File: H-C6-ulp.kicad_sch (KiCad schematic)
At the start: 80 parts, among them J1 USB_C_Receptacle_USB2.0, J2 AFC24-S24FIC-00, J3 SM02B-SRSS-TB(LF)(SN), J4 SM04B-SRSS-TB_LF__SN_, J5 OLED, Q1 Si1308, Q2 Si2301CDS, SW1 SW_Push_Dual, SW2 SW_Push_Dual, U1 ESP32-C6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

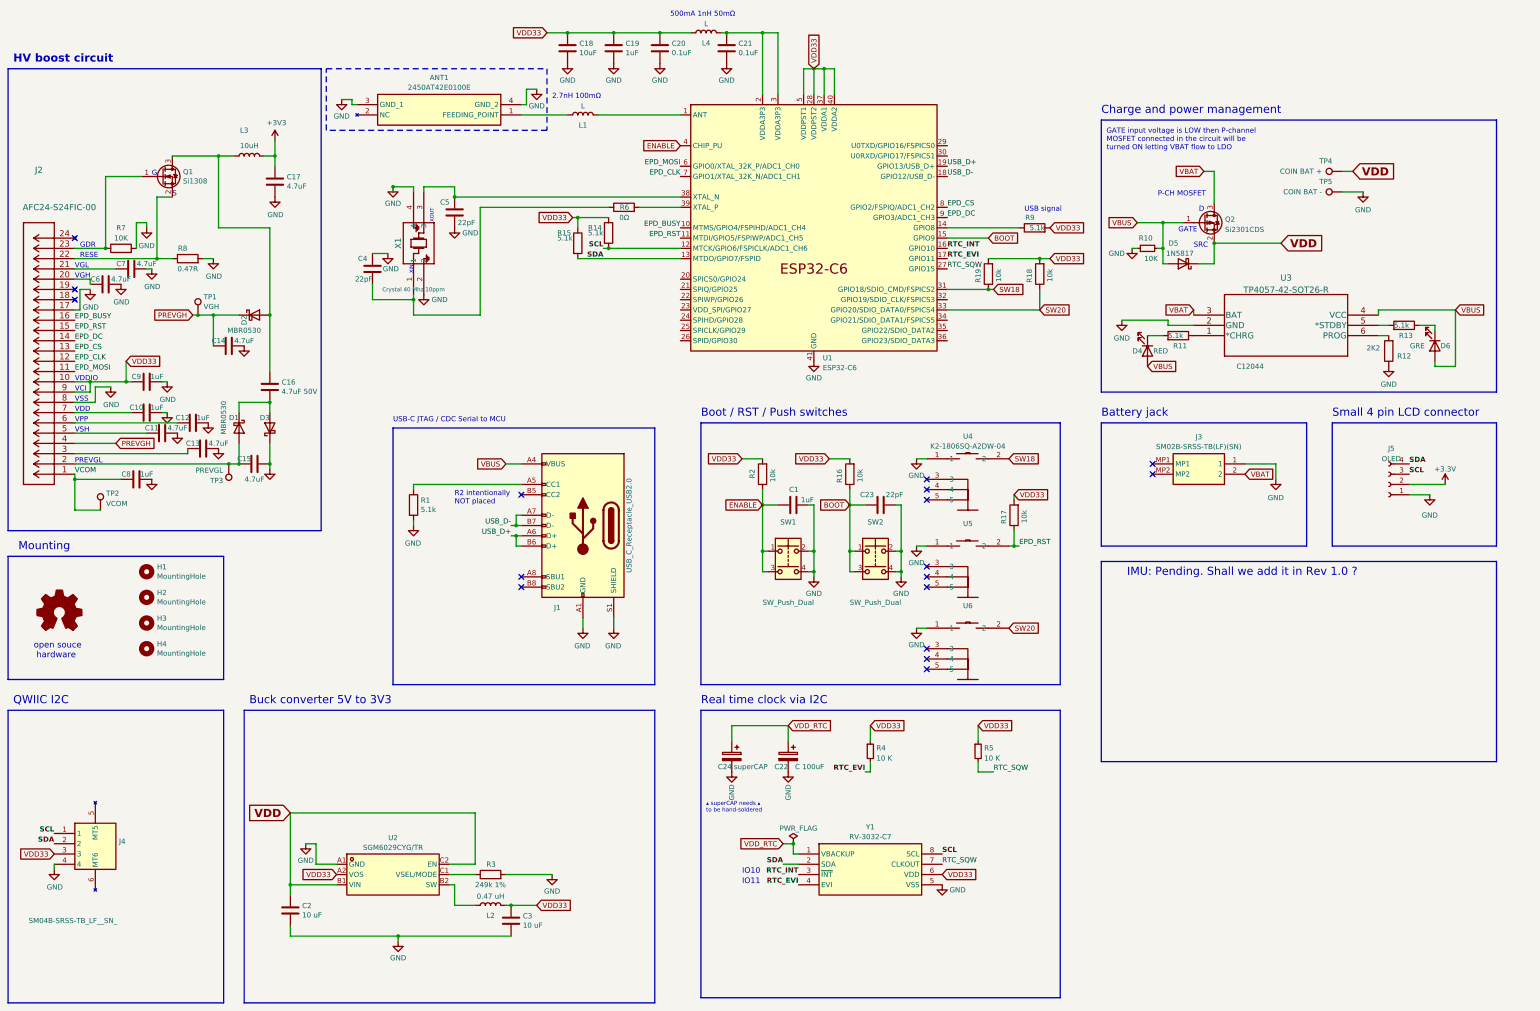
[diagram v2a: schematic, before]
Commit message: Add QSPI Flash
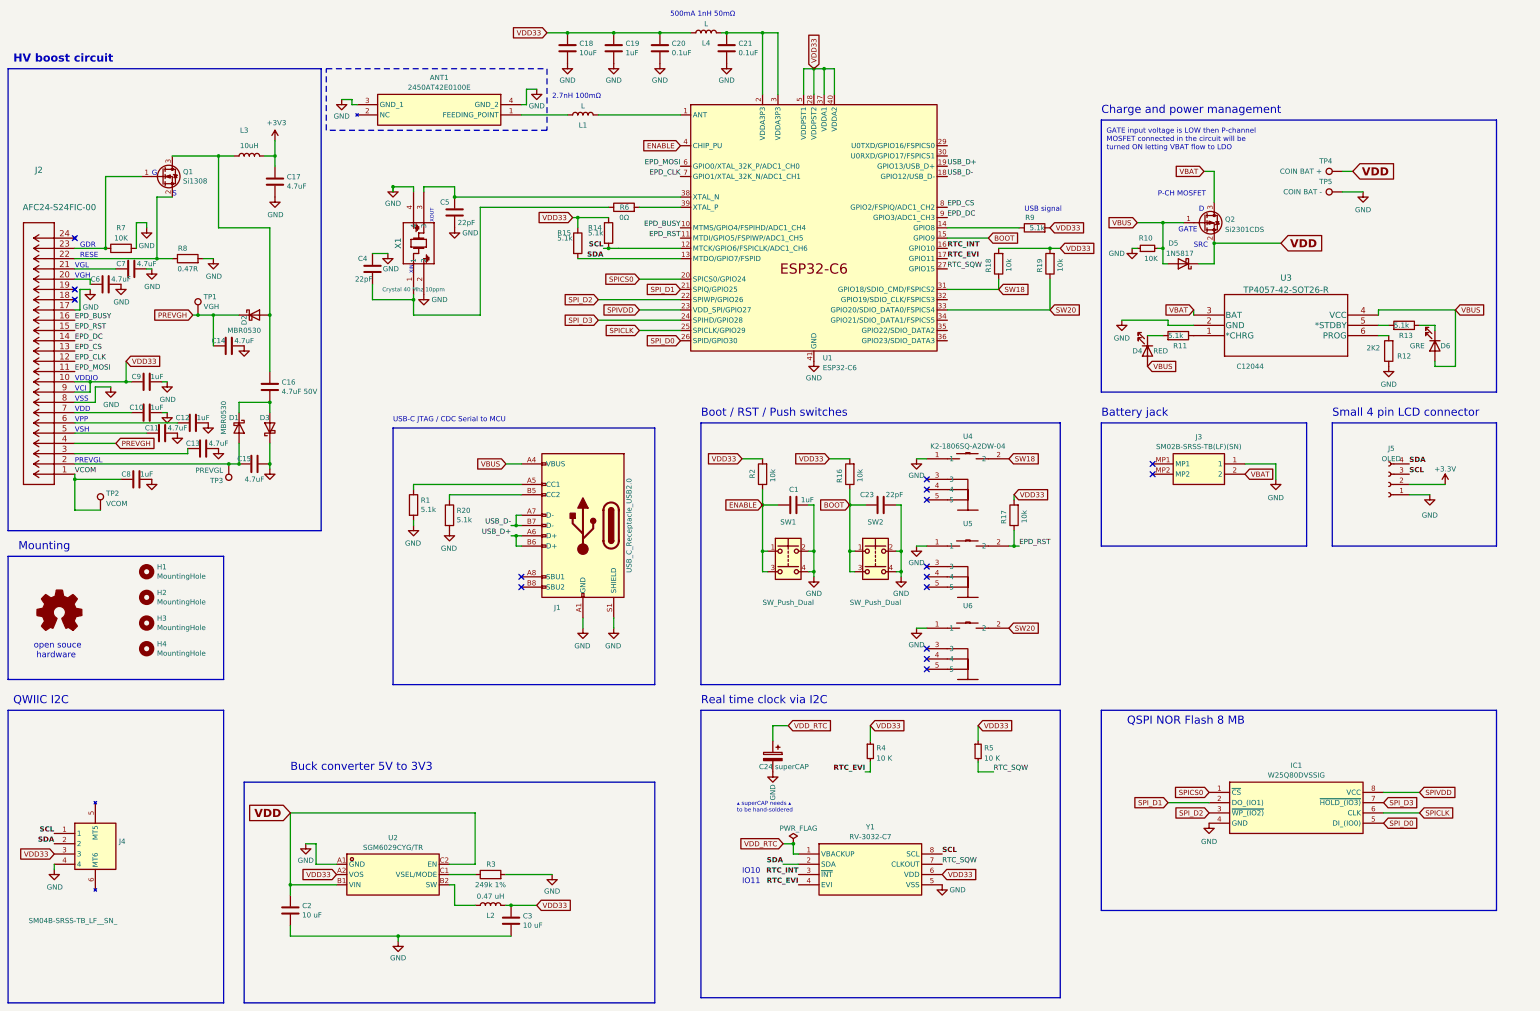
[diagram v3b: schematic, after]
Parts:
- removed C22: C 100uF, Capacitor_Tantalum_SMD:CP_EIA-3528-21_Kemet-B, symbol Device:C_Polarized
- added IC1: W25Q80DVSSIG, footprints:SOIC127P790X216-8N-FLASH, symbol FLASH:W25Q80DVSSIG
- added R20: 5.1k, Resistor_SMD:R_0603_1608Metric, symbol Device:R
- ANT1: Arrow Part Number 2450AT42E0100E -> (none); Arrow Price/Stock https://www.arrow.com/en/products/2450at42e0100e/johanson-d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 -> (none); Manufacturer_Name JOHANSON TECHNOLOGY -> (none); Manufacturer_Part_Number 2450AT42E0100E -> (none); Mouser Part Number 609-2450AT42E0100E -> (none); Mouser Price/Stock https://www.mouser.co.uk/ProductDetail/Johanson-Technology/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 -> (none)
- C1, C19: footprint Capacitor_SMD:C_0603_1608Metric -> Capacitor_SMD:C_0402_1005Metric; LCSC C5457064 -> C162161
- C2, C3: LCSC C5457064 -> C6119874
- C23, C4, C5: footprint Capacitor_SMD:C_0603_1608Metric -> Capacitor_SMD:C_0402_1005Metric; LCSC C561172 -> C5119318
- R10, R4, R5: footprint Resistor_SMD:R_0603_1608Metric -> Resistor_SMD:R_0402_1005Metric; LCSC C25804 -> C4322213
- R7: LCSC C25804 -> C4322213
- U1: LCSC C5364646 -> C5364646
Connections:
- net GND: now also IC1.4 (GND), R20.2
- net SW18: now also R18.1; no longer R19.1
- net SW20: now also R19.1; no longer R18.1
- net at J1.B5 (CC2): now also R20.1
- net SPICS0: now reaches U1.20 (SPICS0/GPIO24)
- net SPICS0: now also IC1.1 (~{CS})
- net SPI_D1: now reaches U1.21 (SPIQ/GPIO25)
- net SPI_D1: now also IC1.2 (DO_(IO1))
- net SPI_D2: now reaches U1.22 (SPIWP/GPIO26)
- net SPI_D2: now also IC1.3 (~{WP_(IO2)})
- net SPIVDD: now reaches U1.23 (VDD_SPI/GPIO27)
- net SPIVDD: now also IC1.8 (VCC)
- net SPI_D3: now reaches U1.24 (SPIHD/GPIO28)
- net SPI_D3: now also IC1.7 (~{HOLD_(IO3)})
- net SPICLK: now reaches U1.25 (SPICLK/GPIO29)
- net SPICLK: now also IC1.6 (CLK)
- net SPI_D0: now reaches U1.26 (SPID/GPIO30)
- net SPI_D0: now also IC1.5 (DI_(IO0))
- no-connect marks 17 -> 16
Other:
- note added: "QSPI NOR Flash 8 MB"
- note removed: "IMU: Pending. Shall we add it in Rev 1.0 ?"
- note removed: "R2 intentionally NOT placed"
- moved on the sheet: C24

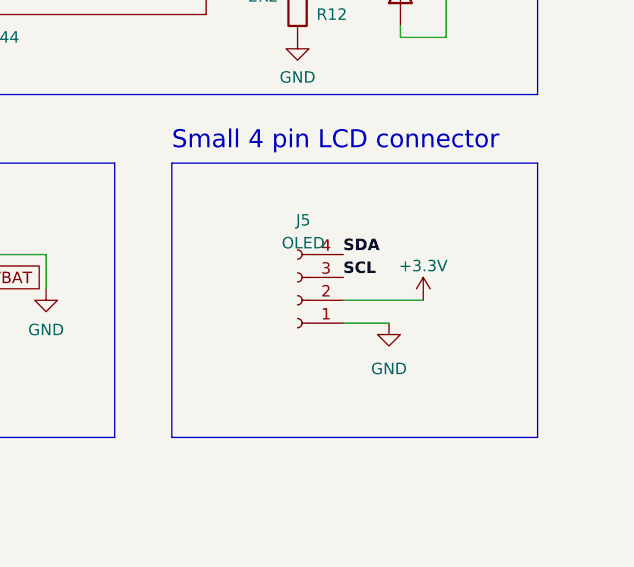
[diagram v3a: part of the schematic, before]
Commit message: Test with external flash
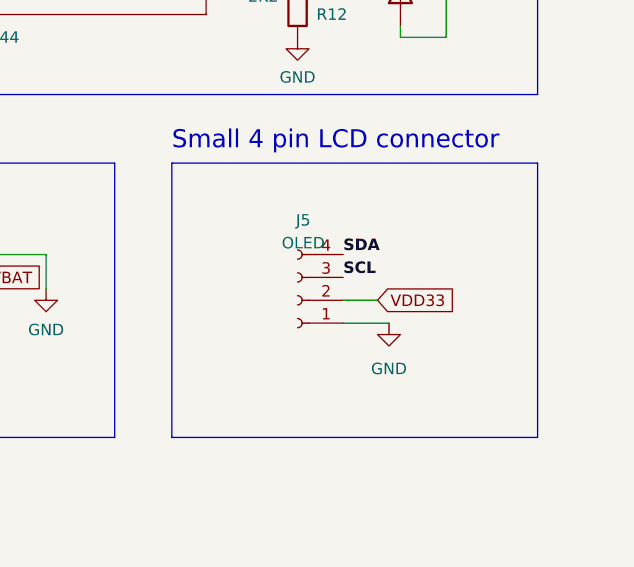
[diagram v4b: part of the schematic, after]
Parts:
- IC1: Arrow Part Number W25Q80DVSSIG -> (none); Arrow Price/Stock https://www.arrow.com/en/products/w25q80dvssig/winbond-elec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 -> (none); LCSC (none) -> C14086; Manufacturer_Part_Number W25Q80DVSSIG -> (none); Mouser Part Number 454-W25Q80DVSSIG -> (none); Mouser Price/Stock https://www.mouser.co.uk/ProductDetail/Winbond/W25Q80DVSSIG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 -> (none)
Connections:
- net +3.3V is gone; now on net VDD33: J5.2 (Pin_2)
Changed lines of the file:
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@@
     (stroke (width 0) (type default))
   )
-  (wire (pts (xy 367.03 144.78) (xy 375.92 144.78))
-    (stroke (width 0) (type default))
-  )
   (wire (pts (xy 71.12 110.49) (xy 71.12 102.87))
     (stroke (width 0) (type default))
@@
     (stroke (width 0) (type default))
   )
+  (wire (pts (xy 370.84 144.78) (xy 367.03 144.78))
+    (stroke (width 0) (type default))
+  )
   (wire (pts (xy 232.41 215.9) (xy 233.68 215.9))
     (stroke (width 0) (type default))
@@
     )
   )
+  (global_label "VDD33" (shape input) (at 370.84 144.78 0) (fields_autoplaced)
+    (effects (font (size 1.27 1.27)) (justify left))
+    (property "Intersheetrefs" "${INTERSHEET_REFS}" (at 379.8728 144.78 0)
+      (effects (font (size 1.27 1.27)) (justify left) hide)
+    )
+    (property "Referenzen zwischen Schaltplänen" "${INTERSHEET_REFS}" (at 370.84 146.9708 0)
+      (effects (font (size 1.27 1.27)) (justify left) hide)
+    )
+  )
   (global_label "VDD33" (shape input) (at 151.13 248.92 0) (fields_autoplaced)
     (effects (font (size 1.27 1.27)) (justify left))
@@
     )
   )
-  (symbol (lib_id "power:+3.3V") (at 375.92 144.78 0) (unit 1)
-    (in_bom yes) (on_board yes) (dnp no) (fields_autoplaced)
-    (property "Reference" "#PWR048" (at 375.92 148.59 0)
-      (effects (font (size 1.27 1.27)) hide)
-    )
-    (property "Value" "+3.3V" (at 375.92 140.97 0)
-      (effects (font (size 1.27 1.27)))
-    )
-    (property "Footprint" "" (at 375.92 144.78 0)
-      (effects (font (size 1.27 1.27)) hide)
-    )
-    (property "Datasheet" "" (at 375.92 144.78 0)
-      (effects (font (size 1.27 1.27)) hide)
-    )
-    (pin "1")
-    (instances
-      (project "H-C6-ulp"
-        (path "/4820ae53-5724-49d2-a676-459cc31081bd"
-          (reference "#PWR048") (unit 1)
-        )
-      )
-    )
-  )
   (symbol (lib_id "QWIIC:SM04B-SRSS-TB_LF__SN_") (at 31.75 231.14 0) (unit 1)
     (in_bom yes) (on_board yes) (dnp no)
@@
       (effects (font (size 1.27 1.27)) (justify left top) hide)
     )
-    (property "Manufacturer_Part_Number" "W25Q80DVSSIG" (at 356.87 815.9 0)
-      (effects (font (size 1.27 1.27)) (justify left top) hide)
-    )
-    (property "Mouser Part Number" "454-W25Q80DVSSIG" (at 356.87 915.9 0)
-      (effects (font (size 1.27 1.27)) (justify left top) hide)
-    )
-    (property "Mouser Price/Stock" "https://www.mouser.co.uk/ProductDetail/Winbond/W25Q80DVSSIG?qs=qSfuJ%252Bfl%2Fd6z%2FQYNv5lpMA%3D%3D" (at 356.87 1015.9 0)
-      (effects (font (size 1.27 1.27)) (justify left top) hide)
-    )
-    (property "Arrow Part Number" "W25Q80DVSSIG" (at 356.87 1115.9 0)
-      (effects (font (size 1.27 1.27)) (justify left top) hide)
-    )
-    (property "Arrow Price/Stock" "https://www.arrow.com/en/products/w25q80dvssig/winbond-electronics?region=nac" (at 356.87 1215.9 0)
+    (property "LCSC" "C14086" (at 356.87 815.9 0)
       (effects (font (size 1.27 1.27)) (justify left top) hide)
     )

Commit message: C6-ulp-schematic_Rev1.
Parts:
- removed IC1: W25Q80DVSSIG, footprints:SOIC127P790X216-8N-FLASH, symbol FLASH:W25Q80DVSSIG
- removed U1: ESP32-C6, footprints:C6_QFN40P500X500X90-41N-D, symbol Espressif:ESP32-C6
- added TP10: RX, TestPoint:TestPoint_Pad_D1.0mm, symbol Connector:TestPoint
- added TP6: 21, TestPoint:TestPoint_Pad_D1.0mm, symbol Connector:TestPoint
- added TP7: 22, TestPoint:TestPoint_Pad_D1.0mm, symbol Connector:TestPoint
- added TP8: 23, TestPoint:TestPoint_Pad_D1.0mm, symbol Connector:TestPoint
- added TP9: TX, TestPoint:TestPoint_Pad_D1.0mm, symbol Connector:TestPoint
- added U1: ESP32-C6FH4, Package_DFN_QFN:QFN-32-1EP_5x5mm_P0.5mm_EP3.6x3.6mm, symbol Espressif:ESP32-C6FH4
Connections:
- net BOOT: now also U1.15 (GPIO9)
- net ENABLE: now also U1.4 (CHIP_PU)
- net EPD_BUSY: now also U1.10 (MTMS/GPIO4/FSPIHD/ADC1_CH4)
- net EPD_CLK: now also U1.7 (GPIO1/XTAL_32K_N/ADC1_CH1)
- net EPD_CS: now also U1.8 (GPIO2/FSPIQ/ADC1_CH2)
- net EPD_DC: now also U1.9 (GPIO3/ADC1_CH3)
- net EPD_MOSI: now also U1.6 (GPIO0/XTAL_32K_P/ADC1_CH0)
- net EPD_RST: now also U1.11 (MTDI/GPIO5/FSPIWP/ADC1_CH5)
- net GND: now also U1.33 (GND)
- net RTC_EVI: now also U1.19 (GPIO15)
- net RTC_INT: now also U1.18 (GPIO14)
- net RTC_SQW: now also U1.25 (GPIO20/SDIO_DATA0/FSPICS4)
- net SCL: now also U1.12 (MTCK/GPIO6/FSPICLK/ADC1_CH6)
- net SDA: now also U1.13 (MTDO/GPIO7/FSPID)
- net SW18: now also U1.23 (GPIO18/SDIO_CMD/FSPICS2); no longer U4.2
- net SW20: no longer R19.1
- net USB_D+: now also U1.17 (GPIO13/USB_D+)
- net USB_D-: now also U1.16 (GPIO12/USB_D-)
- net VDD33: now also U1.20 (VDDPST2), U1.29 (VDDA1), U1.32 (VDDA2), U1.5 (VDDPST1)
- net at L1.2: now also U1.1 (ANT)
- net at R9.1: now also U1.14 (GPIO8)
- net at C21.2, L4.2: now also U1.2 (VDDA3P3), U1.3 (VDDA3P3)
- net at C5.1, X1.3: now also U1.30 (XTAL_N)
- net at R6.2: now also U1.31 (XTAL_P)
- new net IO_21: TP6.1, U1.26 (GPIO21/SDIO_DATA1/FSPICS5)
- new net IO_22: TP7.1, U1.27 (GPIO22/SDIO_DATA2)
- new net IO_23: TP8.1, U1.28 (GPIO23/SDIO_DATA3)
- new net IO_RX: TP10.1, U1.22 (U0RXD/GPIO17/FSPICS1)
- new net IO_TX: TP9.1, U1.21 (U0TXD/GPIO16/FSPICS0)
- new net SW19: R19.1, U1.24 (GPIO19/SDIO_CLK/FSPICS3), U4.2
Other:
- note added: "SERIAL UART"
- note removed: "QSPI NOR Flash 8 MB"

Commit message: 1.1 ready for review
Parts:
- removed R5: 10 K, Resistor_SMD:R_0402_1005Metric, symbol Device:R_Small
- removed TP4: COIN BAT +, TestPoint:TestPoint_Pad_D1.0mm, symbol Connector:TestPoint
- removed TP5: COIN BAT -, TestPoint:TestPoint_Pad_D1.0mm, symbol Connector:TestPoint
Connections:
- net SW20 is gone; now on net SW19: U6.2
- net RTC_EVI: now also U1.18 (GPIO14); no longer U1.19 (GPIO15)
- net RTC_INT: now also U1.19 (GPIO15); no longer U1.18 (GPIO14)
- net SW18: now also U4.2
- net SW19: no longer U4.2
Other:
- moved on the sheet: D5, Q2, R10

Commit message: Rel 1.1 ready
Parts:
- R10: LCSC C4322213 -> C25804
- R7: footprint Resistor_SMD:R_0603_1608Metric -> Resistor_SMD:R_0402_1005Metric; LCSC C4322213 -> C25804
- U1: LCSC (none) -> C6908287
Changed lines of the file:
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@@
+      (effects (font (size 1.27 1.27)) hide)
+    )
+    (property "LCSC" "C6908287" (at 219.71 81.28 0)
       (effects (font (size 1.27 1.27)) hide)
     )
@@
       (effects (font (size 1.27 1.27)) hide)
     )
-    (property "LCSC" "C4322213" (at 331.47 80.01 90)
+    (property "LCSC" "C25804" (at 331.47 80.01 90)
       (effects (font (size 1.27 1.27)) hide)
     )
@@
       (effects (font (size 1.27 1.27)))
     )
-    (property "Footprint" "Resistor_SMD:R_0603_1608Metric" (at 48.26 88.138 90)
+    (property "Footprint" "Resistor_SMD:R_0402_1005Metric" (at 48.26 88.138 90)
       (effects (font (size 1.27 1.27)) hide)
     )
@@
       (effects (font (size 1.27 1.27)) hide)
     )
-    (property "LCSC" "C4322213" (at 48.26 86.36 90)
-      (effects (font (size 1.27 1.27)) hide)
-    )
+    (property "LCSC" "C25804" (at 48.26 86.36 90)
+      (effects (font (size 1.27 1.27)) hide)
+    )

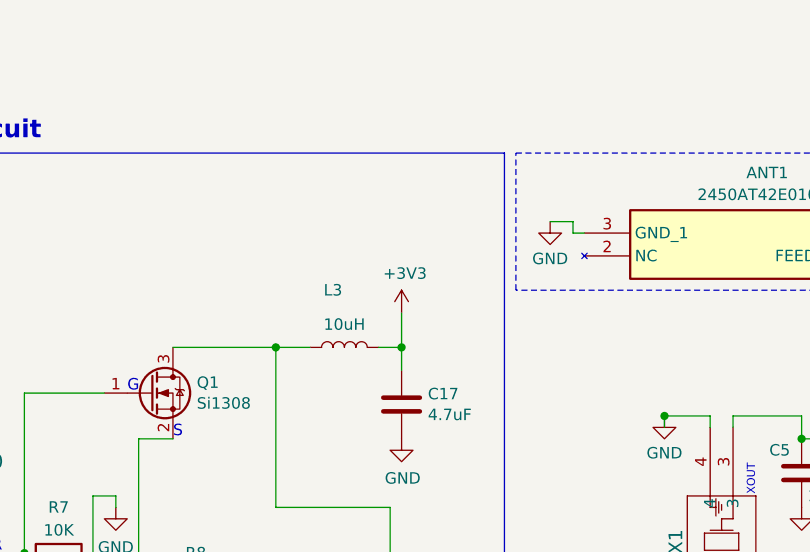
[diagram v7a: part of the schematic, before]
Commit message: Fix epaper power
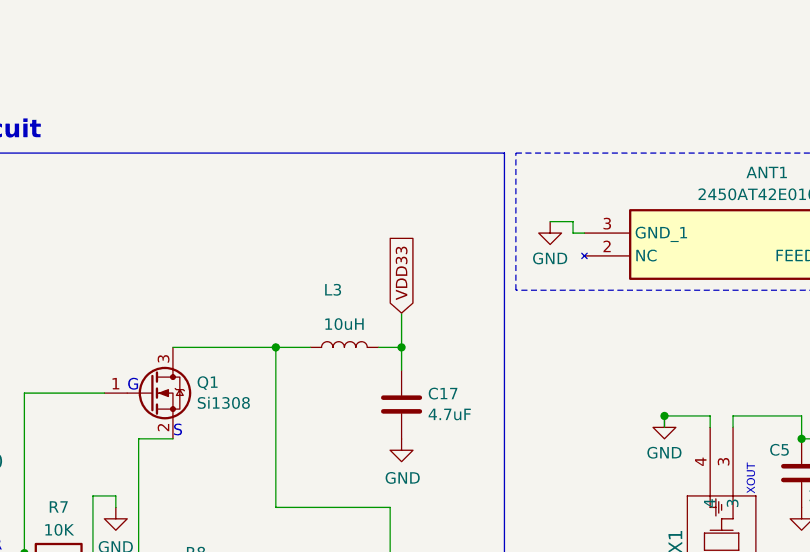
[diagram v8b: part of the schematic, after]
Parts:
- R7: LCSC C25804 -> C4322213
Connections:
- net +3V3 is gone; now on net VDD33: C17.2, L3.2
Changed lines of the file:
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@@
+    )
+  )
+  (global_label "VDD33" (shape input) (at 86.36 59.69 90) (fields_autoplaced)
+    (effects (font (size 1.27 1.27)) (justify left))
+    (property "Intersheetrefs" "${INTERSHEET_REFS}" (at 86.36 50.6572 90)
+      (effects (font (size 1.27 1.27)) (justify left) hide)
+    )
+    (property "Referenzen zwischen Schaltplänen" "${INTERSHEET_REFS}" (at 88.5508 59.69 90)
+      (effects (font (size 1.27 1.27)) (justify left) hide)
     )
   )
@@
     )
   )
-  (symbol (lib_id "power:+3V3") (at 86.36 59.69 0) (unit 1)
-    (in_bom yes) (on_board yes) (dnp no)
-    (property "Reference" "#PWR032" (at 86.36 63.5 0)
-      (effects (font (size 1.27 1.27)) hide)
-    )
-    (property "Value" "+3V3" (at 86.741 55.2958 0)
-      (effects (font (size 1.27 1.27)))
-    )
-    (property "Footprint" "" (at 86.36 59.69 0)
-      (effects (font (size 1.27 1.27)) hide)
-    )
-    (property "Datasheet" "" (at 86.36 59.69 0)
-      (effects (font (size 1.27 1.27)) hide)
-    )
-    (pin "1")
-    (instances
-      (project "H-C6-ulp"
-        (path "/4820ae53-5724-49d2-a676-459cc31081bd"
-          (reference "#PWR032") (unit 1)
-        )
-      )
-    )
-  )
   (symbol (lib_id "Device:L") (at 80.01 63.5 90) (unit 1)
     (in_bom yes) (on_board yes) (dnp no)
@@
       (effects (font (size 1.27 1.27)) hide)
     )
-    (property "LCSC" "C25804" (at 48.26 86.36 90)
-      (effects (font (size 1.27 1.27)) hide)
-    )
+    (property "LCSC" "C4322213" (at 48.26 86.36 90)
+      (effects (font (size 1.27 1.27)) hide)
+    )
